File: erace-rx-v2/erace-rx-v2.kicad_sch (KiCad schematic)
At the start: 59 parts, among them J1 Conn_01x08_MountingPin, J2 USB_C_Receptacle_USB2.0_16P, Q1 2N7002, Q2 2N7002, U1 ESP32-C3, U2 AMS1117-3.3, Y1 40MHz, Y2 52MHz

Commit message: 0 DRC violations :tada:
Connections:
- net GND: now also J1.MP (MountPin)
- net IO9: no longer BN1.2
- net IO18 renamed USBD-
- net IO19 renamed USBD+
- no-connect marks 16 -> 17
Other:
- moved on the sheet: BN1
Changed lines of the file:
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@@
 	)
 	(junction
-		(at 237.49 132.08)
-		(diameter 0)
-		(color 0 0 0 0)
-	)
-	(junction
 		(at 35.56 57.15)
 		(diameter 0)
@@
 	)
 	(junction
-		(at 215.9 152.4)
+		(at 237.49 132.08)
 		(diameter 0)
 		(color 0 0 0 0)
 	)
 	(junction
-		(at 33.02 57.15)
+		(at 215.9 152.4)
 		(diameter 0)
 		(color 0 0 0 0)
@@
 	)
 	(junction
-		(at 34.29 72.39)
+		(at 34.29 74.93)
 		(diameter 0)
 		(color 0 0 0 0)
@@
 	)
 	(no_connect
+		(at 33.02 59.69)
+	)
+	(no_connect
 		(at 109.22 83.82)
 	)
@@
 	(wire
 		(pts
-			(xy 43.18 57.15) (xy 35.56 57.15)
-		)
-		(stroke
-			(width 0)
-			(type default)
-		)
-	)
-	(wire
-		(pts
 			(xy 109.22 161.29) (xy 118.11 161.29)
 		)
@@
 	(wire
 		(pts
-			(xy 33.02 72.39) (xy 34.29 72.39)
+			(xy 33.02 74.93) (xy 34.29 74.93)
 		)
 		(stroke
@@
 	(wire
 		(pts
-			(xy 27.94 57.15) (xy 33.02 57.15)
-		)
-		(stroke
-			(width 0)
-			(type default)
-		)
-	)
-	(wire
-		(pts
 			(xy 224.79 110.49) (xy 232.41 110.49)
 		)
@@
 	(wire
 		(pts
+			(xy 35.56 57.15) (xy 35.56 59.69)
+		)
+		(stroke
+			(width 0)
+			(type default)
+		)
+	)
+	(wire
+		(pts
 			(xy 208.28 33.02) (xy 208.28 35.56)
 		)
@@
 	(wire
 		(pts
-			(xy 43.18 55.88) (xy 43.18 57.15)
+			(xy 35.56 55.88) (xy 35.56 57.15)
 		)
 		(stroke
@@
 	(wire
 		(pts
+			(xy 35.56 57.15) (xy 27.94 57.15)
+		)
+		(stroke
+			(width 0)
+			(type default)
+		)
+	)
+	(wire
+		(pts
 			(xy 81.28 24.13) (xy 86.36 24.13)
 		)
@@
 	(wire
 		(pts
-			(xy 33.02 57.15) (xy 35.56 57.15)
-		)
-		(stroke
-			(width 0)
-			(type default)
-		)
-	)
-	(wire
-		(pts
 			(xy 229.87 29.21) (xy 251.46 29.21)
 		)
@@
 	(wire
 		(pts
-			(xy 34.29 72.39) (xy 35.56 72.39)
+			(xy 34.29 74.93) (xy 35.56 74.93)
 		)
 		(stroke
@@
 	(wire
 		(pts
-			(xy 43.18 55.88) (xy 63.5 55.88)
+			(xy 35.56 55.88) (xy 63.5 55.88)
 		)
 		(stroke
@@
 		)
 	)
-	(label "IO19"
+	(label "USBD+"
 		(at 52.07 63.5 0)
 		(fields_autoplaced yes)
@@
 		)
 	)
-	(label "IO18"
+	(label "USBD-"
 		(at 194.31 43.18 0)
 		(fields_autoplaced yes)
@@
 		)
 	)
-	(label "IO18"
+	(label "USBD-"
 		(at 130.81 78.74 0)
 		(fields_autoplaced yes)
@@
 		)
 	)
-	(label "IO18"
+	(label "USBD-"
 		(at 52.07 60.96 0)
 		(fields_autoplaced yes)
@@
 		)
 	)
-	(label "IO19"
+	(label "USBD+"
 		(at 194.31 48.26 0)
 		(fields_autoplaced yes)
@@
 	)
 	(symbol
+		(lib_id "power:GND")
+		(at 256.54 49.53 0)
+		(unit 1)
+		(exclude_from_sim no)
+		(in_bom yes)
+		(on_board yes)
+		(dnp no)
+		(fields_autoplaced yes)
+		(property "Reference" "#PWR041"
+			(at 256.54 55.88 0)
+			(effects
+				(font
+					(size 1.27 1.27)
+				)
+				(hide yes)
+			)
+		)
+		(property "Value" "GND"
+			(at 256.54 54.61 0)
+			(effects
+				(font
+					(size 1.27 1.27)
+				)
+			)
+		)
+		(property "Footprint" ""
+			(at 256.54 49.53 0)
+			(effects
+				(font
+					(size 1.27 1.27)
+				)
+				(hide yes)
+			)
+		)
+		(property "Datasheet" ""
+			(at 256.54 49.53 0)
+			(effects
+				(font
+					(size 1.27 1.27)
+				)
+				(hide yes)
+			)
+		)
+		(property "Description" "Power symbol creates a global label with name \"GND\" , ground"
+			(at 256.54 49.53 0)
+			(effects
+				(font
+					(size 1.27 1.27)
+				)
+				(hide yes)
+			)
+		)
+		(pin "1"
+		)
+		(instances
+			(project ""
+				(path "/6f78400b-c6a5-4e89-99c3-5503b1f88e0b"
+					(reference "#PWR041")
+					(unit 1)
+				)
+			)
+		)
+	)
+	(symbol
 		(lib_id "power:VCC")
 		(at 72.39 124.46 0)
@@
 	(symbol
 		(lib_id "components:Button")
-		(at 34.29 64.77 270)
+		(at 34.29 67.31 270)
 		(unit 1)
 		(exclude_from_sim no)
@@
 		(fields_autoplaced yes)
 		(property "Reference" "BN1"
-			(at 39.37 64.1349 90)
+			(at 39.37 66.6749 90)
 			(effects
 				(font
@@
 		)
 		(property "Value" "~"
-			(at 39.37 66.04 90)
+			(at 39.37 68.58 90)
 			(effects
 				(font
@@
 		)
 		(property "Footprint" "components:button"
-			(at 33.02 64.77 0)
+			(at 33.02 67.31 0)
 			(effects
 				(font
@@
 		)
 		(property "Datasheet" ""
-			(at 33.02 64.77 0)
+			(at 33.02 67.31 0)
 			(effects
 				(font
@@
 		)
 		(property "Description" ""
-			(at 33.02 64.77 0)
+			(at 33.02 67.31 0)
 			(effects
 				(font
@@
 	(symbol
 		(lib_id "power:GND")
-		(at 34.29 72.39 0)
+		(at 34.29 74.93 0)
 		(unit 1)
 		(exclude_from_sim no)
@@
 		(fields_autoplaced yes)
 		(property "Reference" "#PWR017"
-			(at 34.29 78.74 0)
+			(at 34.29 81.28 0)
 			(effects
 				(font
@@
 		)
 		(property "Value" "GND"
-			(at 34.29 77.47 0)
+			(at 34.29 80.01 0)
 			(effects
 				(font
@@
 		)
 		(property "Footprint" ""
-			(at 34.29 72.39 0)
+			(at 34.29 74.93 0)
 			(effects
 				(font
@@
 		)
 		(property "Datasheet" ""
-			(at 34.29 72.39 0)
+			(at 34.29 74.93 0)
 			(effects
 				(font
@@
 		)
 		(property "Description" "Power symbol creates a global label with name \"GND\" , ground"
-			(at 34.29 72.39 0)
+			(at 34.29 74.93 0)
 			(effects
 				(font

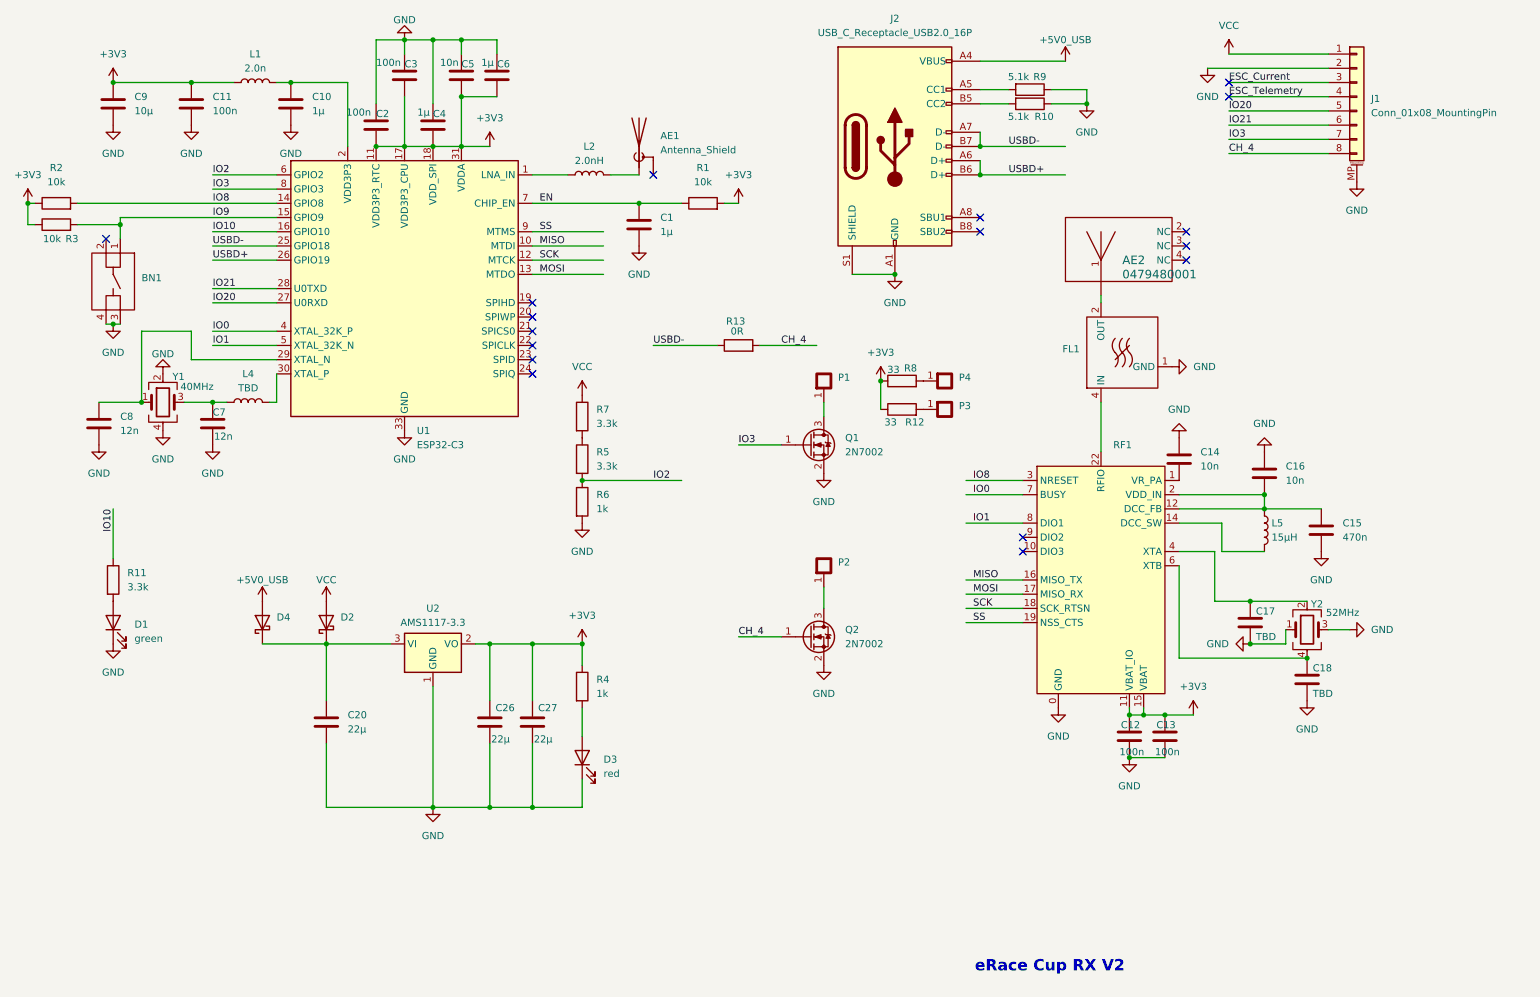
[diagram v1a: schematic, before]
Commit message: corrected XTAL, updated for JLC stock
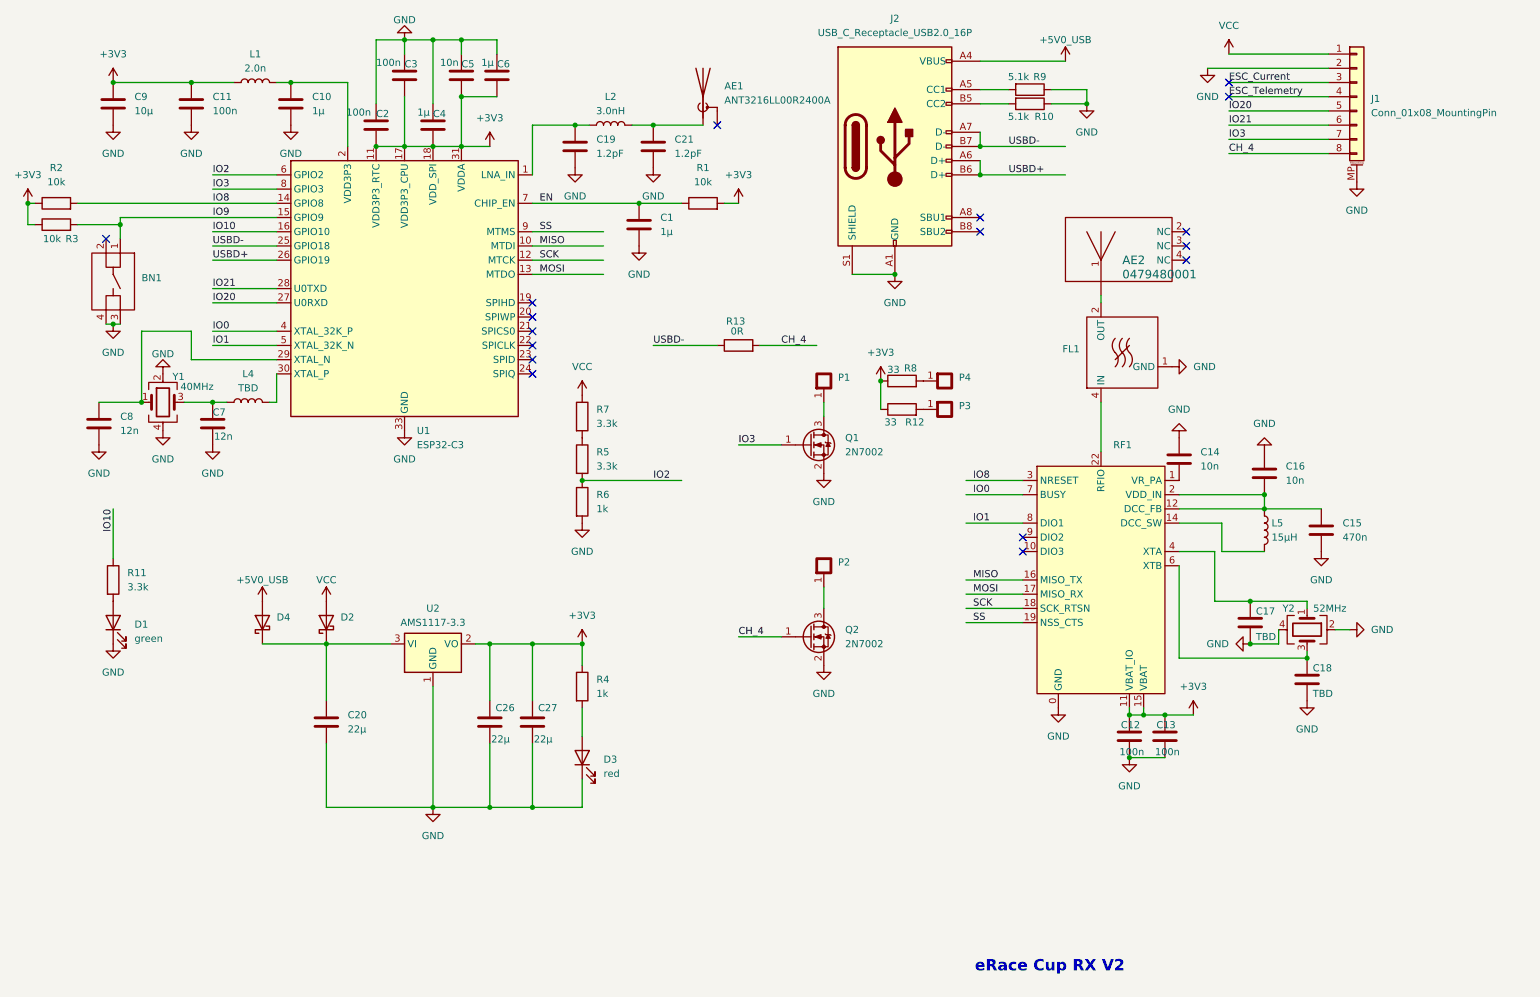
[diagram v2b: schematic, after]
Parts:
- added C19, C21: 1.2pF, Capacitor_SMD:C_0402_1005Metric, symbol Device:C
- AE1: value Antenna_Shield -> ANT3216LL00R2400A
- C15: footprint Capacitor_SMD:C_0402_1005Metric -> Capacitor_SMD:C_0603_1608Metric
- L2: value 2.0nH -> 3.0nH
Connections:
- net GND: now also Y2.2, Y2.4, C19.1, C21.2; no longer Y2.1, Y2.3
- net at C17.1, RF1.4 (XTA): now also Y2.1; no longer Y2.2
- net at C18.1, RF1.6 (XTB): now also Y2.3; no longer Y2.4
- net at L2.1, U1.1 (LNA_IN): now also C19.2
- net at AE1.1 (A), L2.2: now also C21.1
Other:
- moved on the sheet: AE1

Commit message: adjusted for Johanson filter, moved power LED
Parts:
- removed C17, C18: TBD, Capacitor_SMD:C_0402_1005Metric, symbol Device:C
- removed L4: TBD, Inductor_SMD:L_0402_1005Metric, symbol Device:L
- removed R13: 0R, Resistor_SMD:R_0402_1005Metric, symbol Device:R
- added JP1: Jumper_2_Small_Open, components:solder bridge, symbol Jumper:Jumper_2_Small_Open
- AE2: value 0479480001 -> 479480001
- FL1: value ~ -> 2450FM07D0034T
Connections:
- net CH_4: now also JP1.2 (B)
- net USBD-: now also JP1.1 (A)
- net at C7.1, Y1.3: now also U1.30 (XTAL_P)
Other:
- note added: "eRace Cup RX V2.1"
- note removed: "eRace Cup RX V2"
- moved on the sheet: AE2, C12, C13, C14, C15, C16, C20, C26, C27, D1, D2, D3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
